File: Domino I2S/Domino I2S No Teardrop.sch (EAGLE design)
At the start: 56 parts, among them J1 MH4-1, J2 MIC-45-22, J3 MH4-1, J4 MH2-1, J5 MH4-1, J6 DLT1120A, J7 MH4-1, J8 MH2-1, U1 WM8978CGEFL

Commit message: Domino I2S Rev. A: added mounting hole and silkscreen artwork
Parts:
- removed HEADPHONE1: ST-3538-050, Domino:ST-3538-050
- removed J7: MH4-1, Domino:MH4-1
- removed J8: MH2-1, Domino:MH2-1
- removed R19: 10k, Domino:RES_0402
- added MIC1: MIC-45-22, Domino:MIC-45-22
- added R15: 22R, Domino:RES_0402
- C1: value 4u7 -> 1u; PARTNO C0402_4u7_X5R_10%_CER_6V3 -> C0402_1u_X7R_10%_CER_25V; TC X5R -> X7R; VOLT 6.3V -> 25V
- C10: value 1n -> 220p; PARTNO C0402_1n_X7R_10%_CER_50V -> C0402_220p_X7R_10%_CER_50V
- C11: value 1n -> 10n; PARTNO C0402_1n_X7R_10%_CER_50V -> C0402_10n_X7R_10%_CER_50V
- C12: value 33p -> 1u; PARTNO C0402_33p_NP0_5%_CER_50V -> C0402_1u_X7R_10%_CER_25V; TC NP0 -> X7R; TOL ±5% -> ±10%; VOLT 50V -> 25V
- C13: value 1u -> 10n; PARTNO C0402_1u_X7R_10%_CER_25V -> C0402_10n_X7R_10%_CER_50V; VOLT 25V -> 50V
- C14: value 10n -> 1u; PARTNO C0402_10n_X7R_10%_CER_50V -> C0402_1u_X7R_10%_CER_25V; VOLT 50V -> 25V
- C15: value 10n -> 4u7; PARTNO C0402_10n_X7R_10%_CER_50V -> C0402_4u7_X5R_10%_CER_6V3; TC X7R -> X5R; VOLT 50V -> 6.3V
- C16, C9: value 1u -> 4u7; PARTNO C0402_1u_X7R_10%_CER_25V -> C0402_4u7_X5R_10%_CER_6V3; TC X7R -> X5R; VOLT 25V -> 6.3V
- C2, C3: value 4u7 -> 33p; PARTNO C0402_4u7_X5R_10%_CER_6V3 -> C0402_33p_NP0_5%_CER_50V; TC X5R -> NP0; TOL ±10% -> ±5%; VOLT 6.3V -> 50V
- C4, C5: value 4u7 -> 1n; PARTNO C0402_4u7_X5R_10%_CER_6V3 -> C0402_1n_X7R_10%_CER_50V; TC X5R -> X7R; VOLT 6.3V -> 50V
- C7: value 220p -> 4u7; PARTNO C0402_220p_X7R_10%_CER_50V -> C0402_4u7_X5R_10%_CER_6V3; TC X7R -> X5R; VOLT 50V -> 6.3V
- C8: value 33p -> 4u7; PARTNO C0402_33p_NP0_5%_CER_50V -> C0402_4u7_X5R_10%_CER_6V3; TC NP0 -> X5R; TOL ±5% -> ±10%; VOLT 50V -> 6.3V
- J1: value MH4-1 -> DLT1120A; device Domino:MH4-1 -> Domino:DLT1120A; PARTNO (none) -> DLT1120A
- J2: value MIC-45-22 -> ST-3538-050; device Domino:MIC-45-22 -> Domino:ST-3538-050; PARTNO MIC-45-22 -> (none)
- J3: value MH4-1 -> MH2-1; device Domino:MH4-1 -> Domino:MH2-1; DNP (none) -> T; PARTNO (none) -> MH2-1-0.1
- J4: DNP (none) -> T; PARTNO (none) -> MH2-1-0.1
- J5: value MH4-1 -> MH8-1; device Domino:MH4-1 -> Domino:MH8-1
- J6: value DLT1120A -> MH8-1; device Domino:DLT1120A -> Domino:MH8-1; PARTNO DLT1120A -> (none)
- R1: DNP T -> (none)
- R10: value 0R -> 22R; PARTNO R0402_0R_5%_62.5mW -> R0402_22R_5%_62.5mW
- R11, R12: value 4k7 -> 22R; PARTNO R0402_4k7_5%_62.5mW -> R0402_22R_5%_62.5mW
- R14: value 10k -> 22R; DNP T -> (none); PARTNO R0402_10k_5%_62.5mW -> R0402_22R_5%_62.5mW
- R16: value 0R -> 10k; PARTNO R0402_0R_5%_62.5mW -> R0402_10k_5%_62.5mW
- R17: value 0R -> 10k; DNP (none) -> T; PARTNO R0402_0R_5%_62.5mW -> R0402_10k_5%_62.5mW
- R18: value 10k -> 0R; PARTNO R0402_10k_5%_62.5mW -> R0402_0R_5%_62.5mW
- R2: value 0R -> 4k7; PARTNO R0402_0R_5%_62.5mW -> R0402_4k7_5%_62.5mW
- R3: value 22R -> 4k7; PARTNO R0402_22R_5%_62.5mW -> R0402_4k7_5%_62.5mW
- R4, R8: value 22R -> 0R; PARTNO R0402_22R_5%_62.5mW -> R0402_0R_5%_62.5mW
- R5: value 47k -> 0R; DNP (none) -> T; PARTNO R0402_47k_5%_62.5mW -> R0402_0R_5%_62.5mW
- R6: value 22R -> 680R; PARTNO R0402_22R_5%_62.5mW -> R0402_680R_5%_62.5mW
- R7: value 680R -> 47k; PARTNO R0402_680R_5%_62.5mW -> R0402_47k_5%_62.5mW
- R9: value 22R -> 10k; PARTNO R0402_22R_5%_62.5mW -> R0402_10k_5%_62.5mW
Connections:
- net +3V3: now also C15.1, C16.1, C6.1, FB6.2, R1.1, R16.2, R4.1, R9.2; no longer C1.1, C3.1, C4.1, FB3.2, R16.1, R18.2, R19.2, R2.1
- net +5V: now also FB3.1, R5.1; no longer FB4.1, R1.1
- net ADCDAT: now also J6.3, R12.1; no longer J1.2, R6.1
- net BCLK: now also J6.7, R11.1; no longer J3.2, R4.1
- net CSB: now also R18.1; no longer R17.1
- net DACDAT: now also J6.5, R14.1; no longer J3.4, R8.1
- net GND: now also C13.2, C16.2, C3.1, C5.2, C7.1, C9.2, FB4.2, J1.GND, J2.S1, J2.S2, R17.1, R2.2, R3.2, R7.1, R8.1; no longer C1.2, C12.1, C14.2, C3.2, C5.1, C7.2, FB6.2, HEADPHONE1.S1, HEADPHONE1.S2, J6.GND, R10.1, R11.2, R12.2, R14.1, R5.1
- net LOUT1: now also C5.1; no longer C10.1
- net LOUT2: now also L1.1; no longer L2.1
- net LRCK: now also J6.6, R10.1; no longer J3.3, R3.1
- net MCLK: now also J6.4, R15.1; no longer J1.1, R9.1
- net MICBIAS: now also C9.1, R6.2; no longer C6.1, R7.2
- net MICN: now also C14.2, J4.1, MIC1.-, R8.2; no longer C13.2, J2.-, J8.2, R10.2
- net MICP: now also C10.1, C12.2, J4.2, MIC1.+, R6.1, R7.2; no longer C7.1, C9.2, J2.+, J8.1, R5.2, R7.1
- net MODE: now also R16.1, R17.2; no longer R13.1, R14.2
- net N$1: now also R10.2; no longer R3.2
- net N$10: now also FB4.1, J6.1; no longer FB6.1, J1.4
- net N$11: now also FB3.2, J5.1; no longer FB4.2, J5.4
- net N$12: now also R3.1; no longer R11.1
- net N$13: now also R2.1; no longer R12.1
- net N$14: now also FB6.1, J6.8; no longer FB3.1, J3.1
- net N$15: now also J5.6; no longer J7.3
- net N$16: now also C3.2, J2.SW, J2.T; no longer C8.2, HEADPHONE1.SW, HEADPHONE1.T
- net N$17: now also C2.2, J2.R; no longer C12.2, HEADPHONE1.R
- net N$2: now also R11.2; no longer R4.2
- net N$3: now also R12.2; no longer R6.2
- net N$4: now also R14.2; no longer R8.2
- net N$5: now also R15.2; no longer R9.2
- net N$6: now also C12.1; no longer C9.1
- net N$7: now also C14.1; no longer C13.1
- net N$8: now also C1.1, J1.VIN; no longer C16.1, J6.VIN
- net N$9: now also J1.VCC, R1.2; no longer J6.VCC, R16.2
- net ROUT1: now also C4.1; no longer C11.1
- net ROUT2: now also L2.1; no longer L1.1
- net SCLK: now also J5.4, R13.1; no longer J5.1, R18.1
- net SDIN: now also J5.5, R9.1; no longer J7.4, R19.1
- net SPDIF_OUT: now also C1.2, J6.2, R18.2; no longer C16.2, J1.3, R17.2
- net SPKL: now also C11.1, J3.1, L1.2; no longer C15.1, J4.2, L2.2
- net SPKR: now also C13.1, J3.2, L2.2; no longer C14.1, J4.1, L1.2
- net SPKVDD: now also C7.2, R4.2, R5.2; no longer C2.2, R1.2, R2.2
- net VMID: now also C8.2; no longer C5.2
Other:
- note added: "3x"
- note added: "5x"
- moved on the sheet: C1, C10, C11, C12, C13, C14, C15, C16, C2, C3, C4, C5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

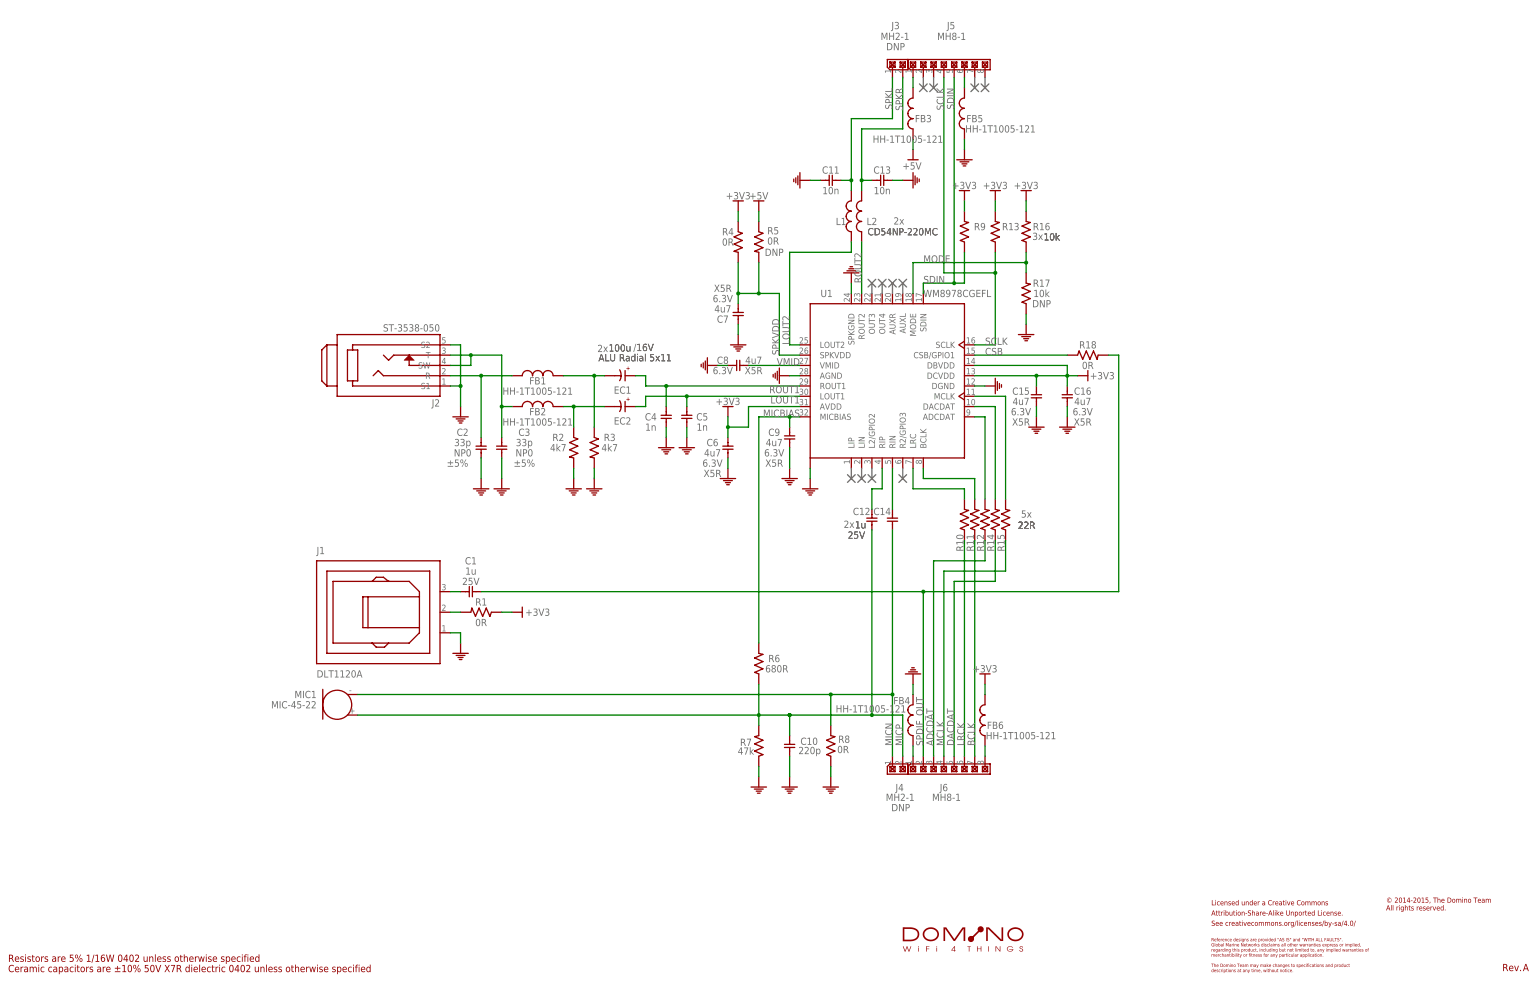
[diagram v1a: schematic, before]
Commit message: Domino I2S Rev. A: started again from correct PADS files
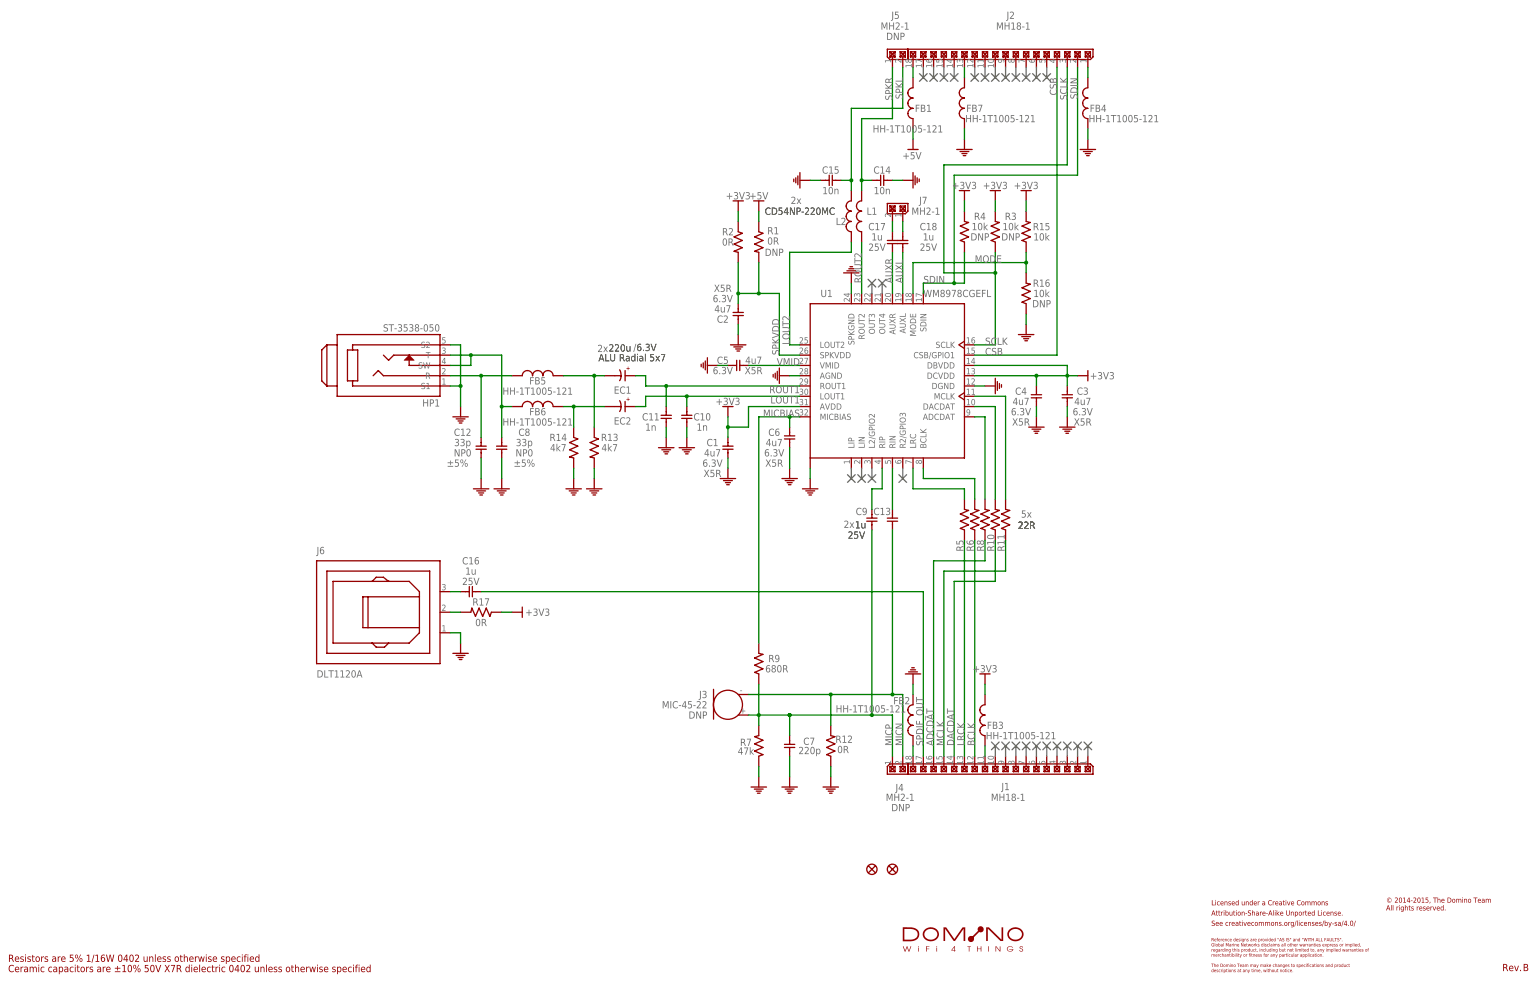
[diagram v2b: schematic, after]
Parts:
- removed MIC1: MIC-45-22, Domino:MIC-45-22
- removed R18: 0R, Domino:RES_0402
- added C17, C18: 1u, Domino:CAP_0402
- added F1, F2: FIDUCIAL, Domino:FIDUCIAL
- added FB7: HH-1T1005-121, Domino:FB_0805
- added HP1: ST-3538-050, Domino:ST-3538-050
- added J7: MH2-1, Domino:MH2-1
- C1: value 1u -> 4u7; PARTNO C0402_1u_X7R_10%_CER_25V -> C0402_4u7_X5R_10%_CER_6V3; TC X7R -> X5R; VOLT 25V -> 6.3V
- C10: value 220p -> 1n; PARTNO C0402_220p_X7R_10%_CER_50V -> C0402_1n_X7R_10%_CER_50V
- C11: value 10n -> 1n; PARTNO C0402_10n_X7R_10%_CER_50V -> C0402_1n_X7R_10%_CER_50V
- C12: value 1u -> 33p; PARTNO C0402_1u_X7R_10%_CER_25V -> C0402_33p_NP0_5%_CER_50V; TC X7R -> NP0; TOL ±10% -> ±5%; VOLT 25V -> 50V
- C13: value 10n -> 1u; PARTNO C0402_10n_X7R_10%_CER_50V -> C0402_1u_X7R_10%_CER_25V; VOLT 50V -> 25V
- C14: value 1u -> 10n; PARTNO C0402_1u_X7R_10%_CER_25V -> C0402_10n_X7R_10%_CER_50V; VOLT 25V -> 50V
- C15: value 4u7 -> 10n; PARTNO C0402_4u7_X5R_10%_CER_6V3 -> C0402_10n_X7R_10%_CER_50V; TC X5R -> X7R; VOLT 6.3V -> 50V
- C16, C9: value 4u7 -> 1u; PARTNO C0402_4u7_X5R_10%_CER_6V3 -> C0402_1u_X7R_10%_CER_25V; TC X5R -> X7R; VOLT 6.3V -> 25V
- C2, C3: value 33p -> 4u7; PARTNO C0402_33p_NP0_5%_CER_50V -> C0402_4u7_X5R_10%_CER_6V3; TC NP0 -> X5R; TOL ±5% -> ±10%; VOLT 50V -> 6.3V
- C4, C5: value 1n -> 4u7; PARTNO C0402_1n_X7R_10%_CER_50V -> C0402_4u7_X5R_10%_CER_6V3; TC X7R -> X5R; VOLT 50V -> 6.3V
- C7: value 4u7 -> 220p; PARTNO C0402_4u7_X5R_10%_CER_6V3 -> C0402_220p_X7R_10%_CER_50V; TC X5R -> X7R; VOLT 6.3V -> 50V
- C8: value 4u7 -> 33p; PARTNO C0402_4u7_X5R_10%_CER_6V3 -> C0402_33p_NP0_5%_CER_50V; TC X5R -> NP0; TOL ±10% -> ±5%; VOLT 6.3V -> 50V
- EC1, EC2: value 100u -> 220u; device Domino:CPOL_E2-5X11 -> Domino:CPOL_E2-5X7; PARTNO (none) -> C2-5x7_220u_ALU_20%_RAD_6V3; TOL (none) -> ±20%; VOLT 16V -> 6.3V
- FB1, FB2, FB3, FB4, FB5, FB6: PARTNO (none) -> HH-1T1005-121
- J1: value DLT1120A -> MH18-1; device Domino:DLT1120A -> Domino:MH18-1; PARTNO DLT1120A -> MH18-1-0.1
- J2: value ST-3538-050 -> MH18-1; device Domino:ST-3538-050 -> Domino:MH18-1; PARTNO (none) -> MH18-1-0.1
- J3: value MH2-1 -> MIC-45-22; device Domino:MH2-1 -> Domino:MIC-45-22; PARTNO MH2-1-0.1 -> MIC-45-22
- J5: value MH8-1 -> MH2-1; device Domino:MH8-1 -> Domino:MH2-1; DNP (none) -> T; PARTNO (none) -> MH2-1-0.1
- J6: value MH8-1 -> DLT1120A; device Domino:MH8-1 -> Domino:DLT1120A; PARTNO (none) -> DLT1120A
- L1, L2: PARTNO (none) -> CD54NP-220MC
- R1, R16: DNP (none) -> T
- R12: value 22R -> 0R; PARTNO R0402_22R_5%_62.5mW -> R0402_0R_5%_62.5mW
- R13: value 10k -> 4k7; PARTNO R0402_10k_5%_62.5mW -> R0402_4k7_5%_62.5mW
- R14: value 22R -> 4k7; PARTNO R0402_22R_5%_62.5mW -> R0402_4k7_5%_62.5mW
- R15: value 22R -> 10k; PARTNO R0402_22R_5%_62.5mW -> R0402_10k_5%_62.5mW
- R17: value 10k -> 0R; DNP T -> (none); PARTNO R0402_10k_5%_62.5mW -> R0402_0R_5%_62.5mW
- R2: value 4k7 -> 0R; PARTNO R0402_4k7_5%_62.5mW -> R0402_0R_5%_62.5mW
- R3: value 4k7 -> 10k; DNP (none) -> T; PARTNO R0402_4k7_5%_62.5mW -> R0402_10k_5%_62.5mW
- R4: value 0R -> 10k; DNP (none) -> T; PARTNO R0402_0R_5%_62.5mW -> R0402_10k_5%_62.5mW
- R5: value 0R -> 22R; DNP T -> (none); PARTNO R0402_0R_5%_62.5mW -> R0402_22R_5%_62.5mW
- R6: value 680R -> 22R; PARTNO R0402_680R_5%_62.5mW -> R0402_22R_5%_62.5mW
- R8: value 0R -> 22R; PARTNO R0402_0R_5%_62.5mW -> R0402_22R_5%_62.5mW
- R9: value 10k -> 680R; PARTNO R0402_10k_5%_62.5mW -> R0402_680R_5%_62.5mW
- renumbered CC-BY-SA1 to CC-BY-SA101, S1 to S101
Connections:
- new net AUXL: C18.2, U1.AUXL
- new net AUXR: C17.2, U1.AUXR
- new net N$18: FB4.2, J2.1
- new net N$19: C17.1, J7.2
- new net N$20: C18.1, J7.1
- net +3V3: now also C1.1, C3.1, C4.1, FB3.2, R15.2, R17.1, R2.1, R3.2, R4.2; no longer C15.1, C16.1, C6.1, FB6.2, R1.1, R13.2, R16.2, R4.1, R9.2
- net +5V: now also FB1.1, R1.1; no longer FB3.1, R5.1
- net ADCDAT: now also J1.16, R8.1; no longer J6.3, R12.1
- net BCLK: now also J1.12, R6.1; no longer J6.7, R11.1
- net CSB: now also J2.4; no longer R18.1
- net DACDAT: now also J1.14, R10.1; no longer J6.5, R14.1
- net GND: now also C1.2, C12.1, C14.2, C3.2, C5.1, C7.2, FB2.2, FB4.1, FB7.1, HP1.S1, HP1.S2, J6.GND, R12.1, R13.2, R14.2, R16.1; no longer C13.2, C16.2, C3.1, C5.2, C7.1, C9.2, FB4.2, FB5.1, J1.GND, J2.S1, J2.S2, R17.1, R2.2, R3.2, R8.1
- net LOUT1: now also C10.1; no longer C5.1
- net LOUT2: now also L2.1; no longer L1.1
- net LRCK: now also J1.13, R5.1; no longer J6.6, R10.1
- net MCLK: now also J1.15, R11.1; no longer J6.4, R15.1
- net MICBIAS: now also C6.1, R9.2; no longer C9.1, R6.2
- net MICN: now also C13.2, J3.-, J4.2, R12.2; no longer C14.2, J4.1, MIC1.-, R8.2
- net MICP: now also C7.1, C9.2, J3.+, J4.1, R9.1; no longer C10.1, C12.2, J4.2, MIC1.+, R6.1
- net MODE: now also R15.1, R16.2; no longer R16.1, R17.2
- net N$1: now also R5.2; no longer R10.2
- net N$10: now also FB2.1, J1.18; no longer FB4.1, J6.1
- net N$11: now also FB1.2, J2.18; no longer FB3.2, J5.1
- net N$12: now also FB5.2, R13.1; no longer FB1.2, R3.1
- net N$13: now also FB6.2, R14.1; no longer FB2.2, R2.1
- net N$14: now also FB3.1, J1.11; no longer FB6.1, J6.8
- net N$15: now also FB7.2, J2.13; no longer FB5.2, J5.6
- net N$16: now also C8.2, FB6.1, HP1.SW, HP1.T; no longer C3.2, FB2.1, J2.SW, J2.T
- net N$17: now also C12.2, FB5.1, HP1.R; no longer C2.2, FB1.1, J2.R
- net N$2: now also R6.2; no longer R11.2
- net N$3: now also R8.2; no longer R12.2
- net N$4: now also R10.2; no longer R14.2
- net N$5: now also R11.2; no longer R15.2
- net N$6: now also C9.1; no longer C12.1
- net N$7: now also C13.1; no longer C14.1
- net N$8: now also C16.1, J6.VIN; no longer C1.1, J1.VIN
- net N$9: now also J6.VCC, R17.2; no longer J1.VCC, R1.2
- net ROUT1: now also C11.1; no longer C4.1
- net ROUT2: now also L1.1; no longer L2.1
- net SCLK: now also J2.3, R3.1; no longer J5.4, R13.1
- net SDIN: now also J2.2, R4.1; no longer J5.5, R9.1
- net SPDIF_OUT: now also C16.2, J1.17; no longer C1.2, J6.2, R18.2
- net SPKL: now also C15.1, J5.2, L2.2; no longer C11.1, J3.1, L1.2
- net SPKR: now also C14.1, J5.1, L1.2; no longer C13.1, J3.2, L2.2
- net SPKVDD: now also C2.2, R1.2, R2.2; no longer C7.2, R4.2, R5.2
- net VMID: now also C5.2; no longer C8.2
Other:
- note removed: "3x"
- moved on the sheet: C1, C10, C11, C12, C13, C14, C15, C16, C2, C3, C4, C5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
